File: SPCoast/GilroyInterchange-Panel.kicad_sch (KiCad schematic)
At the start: 17 parts, among them U6023 0x22, U6024 0x23

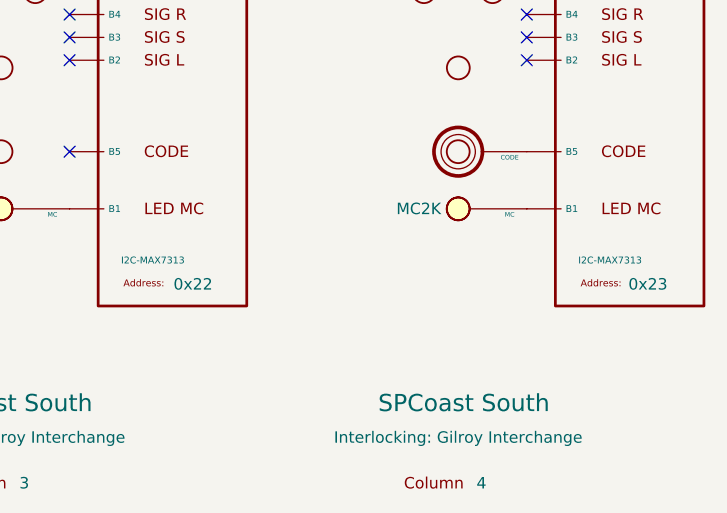
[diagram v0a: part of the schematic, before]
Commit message: chore(kicad): SPCoast symbols refreshed, field attribute visibility, no-connects on unused pins (owner's edit, baseline)
Owner, 2026-10-08: updated symbols from the libraries (the field pin direction flip, InterlockingPlant
61269e0), adjusted attribute visibility, added 22 no-connect markers on unused pins.

Verified (committed as saved, no edits):
- 485 components, 648 nets; every net identical to the previous commit.
- ERC 53 -> 20 messages (13 errors, 7 warnings). Remaining: unconnected HOUSE H / aux MC pins
  (Gilroy Caltrain, Luchessa, Watsonville); Corporal SW11901 still Railroad:Switch_HandThrow (not in
  the library) with open N/R legs; Sargent switch 1 open N/R legs; Christopher Panel U10029 A6 open
  while lamp LMP10093 carries a no-connect; 5 inherited wire stubs.
- Every instance path starts at the root uuid.

Co-Authored-By: Claude Opus 5.5 <noreply@anthropic.com>
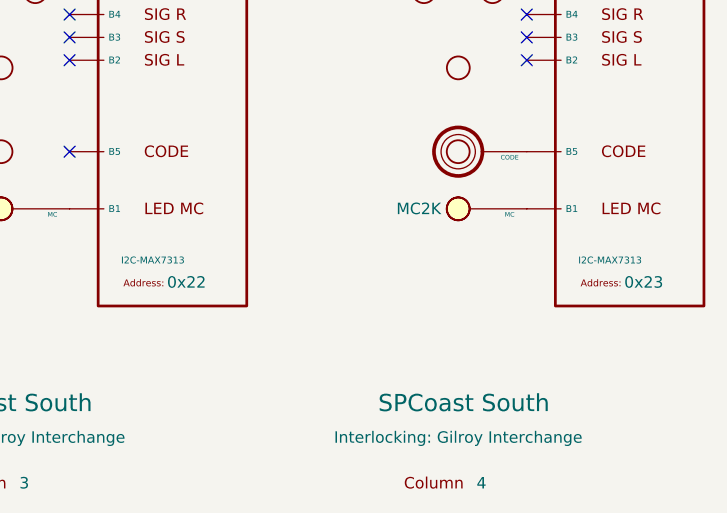
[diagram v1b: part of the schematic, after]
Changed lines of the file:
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@@
+			)
+		)
+		(property "LAMP" ""
+			(at 130.81 26.67 0)
+			(hide yes)
+			(show_name no)
+			(do_not_autoplace no)
+			(effects
+				(font
+					(size 1.27 1.27)
+				)
 			)
 		)
@@
 			)
 		)
+		(property "LAMP" ""
+			(at 80.01 31.75 0)
+			(hide yes)
+			(show_name no)
+			(do_not_autoplace no)
+			(effects
+				(font
+					(size 1.27 1.27)
+				)
+			)
+		)
 		(pin "1"
 		)
@@
 			)
 		)
+		(property "CODE" ""
+			(at 130.81 97.79 0)
+			(hide yes)
+			(show_name no)
+			(do_not_autoplace no)
+			(effects
+				(font
+					(size 1.27 1.27)
+				)
+			)
+		)
 		(pin "1"
 		)
@@
 			)
 		)
+		(property "LAMP" ""
+			(at 80.01 36.83 0)
+			(hide yes)
+			(show_name no)
+			(do_not_autoplace no)
+			(effects
+				(font
+					(size 1.27 1.27)
+				)
+			)
+		)
 		(pin "1"
 		)
@@
 			)
 		)
+		(property "LAMP" ""
+			(at 130.81 104.14 0)
+			(hide yes)
+			(show_name no)
+			(do_not_autoplace no)
+			(effects
+				(font
+					(size 1.27 1.27)
+				)
+			)
+		)
 		(pin "1"
 		)
@@
 			)
 		)
+		(property "WLS" ""
+			(at 130.81 63.5 0)
+			(hide yes)
+			(show_name no)
+			(do_not_autoplace no)
+			(effects
+				(font
+					(size 1.27 1.27)
+				)
+			)
+		)
+		(property "WLK" ""
+			(at 130.81 63.5 0)
+			(hide yes)
+			(show_name no)
+			(do_not_autoplace no)
+			(effects
+				(font
+					(size 1.27 1.27)
+				)
+			)
+		)
 		(pin "1"
 		)
@@
 			)
 		)
+		(property "WLS" ""
+			(at 80.01 63.5 0)
+			(hide yes)
+			(show_name no)
+			(do_not_autoplace no)
+			(effects
+				(font
+					(size 1.27 1.27)
+				)
+			)
+		)
+		(property "WLK" ""
+			(at 80.01 63.5 0)
+			(hide yes)
+			(show_name no)
+			(do_not_autoplace no)
+			(effects
+				(font
+					(size 1.27 1.27)
+				)
+			)
+		)
 		(pin "1"
 		)
@@
 			)
 		)
+		(property "LAMP" ""
+			(at 130.81 36.83 0)
+			(hide yes)
+			(show_name no)
+			(do_not_autoplace no)
+			(effects
+				(font
+					(size 1.27 1.27)
+				)
+			)
+		)
 		(pin "1"
 		)
@@
 			)
 		)
+		(property "SW" ""
+			(at 80.01 48.26 0)
+			(hide yes)
+			(show_name no)
+			(do_not_autoplace no)
+			(effects
+				(font
+					(size 1.27 1.27)
+				)
+			)
+		)
 		(pin "1"
 		)
@@
 			)
 		)
+		(property "LAMP" ""
+			(at 80.01 26.67 0)
+			(hide yes)
+			(show_name no)
+			(do_not_autoplace no)
+			(effects
+				(font
+					(size 1.27 1.27)
+				)
+			)
+		)
 		(pin "1"
 		)
@@
 			(at 144.145 109.855 0)
 			(show_name no)
-			(do_not_autoplace no)
+			(do_not_autoplace yes)
 			(effects
 				(font
@@
 		)
 		(property "Address" "0x23"
-			(at 151.892 112.522 0)
+			(at 151.4281 112.3109 0)
 			(show_name no)
 			(do_not_autoplace no)
@@
 			(at 93.345 109.855 0)
 			(show_name no)
-			(do_not_autoplace no)
+			(do_not_autoplace yes)
 			(effects
 				(font
@@
 		)
 		(property "Address" "0x22"
-			(at 101.346 112.522 0)
+			(at 100.6281 112.3109 0)
 			(show_name no)
 			(do_not_autoplace no)
@@
 			)
 		)
+		(property "LAMP" ""
+			(at 80.01 104.14 0)
+			(hide yes)
+			(show_name no)
+			(do_not_autoplace no)
+			(effects
+				(font
+					(size 1.27 1.27)
+				)
+			)
+		)
 		(pin "1"
 		)
@@
 			)
 		)
+		(property "LAMP" ""
+			(at 130.81 31.75 0)
+			(hide yes)
+			(show_name no)
+			(do_not_autoplace no)
+			(effects
+				(font
+					(size 1.27 1.27)
+				)
+			)
+		)
 		(pin "1"
 		)
@@
 			)
 		)
+		(property "SW" ""
+			(at 130.81 48.26 0)
+			(hide yes)
+			(show_name no)
+			(do_not_autoplace no)
+			(effects
+				(font
+					(size 1.27 1.27)
+				)
+			)
+		)

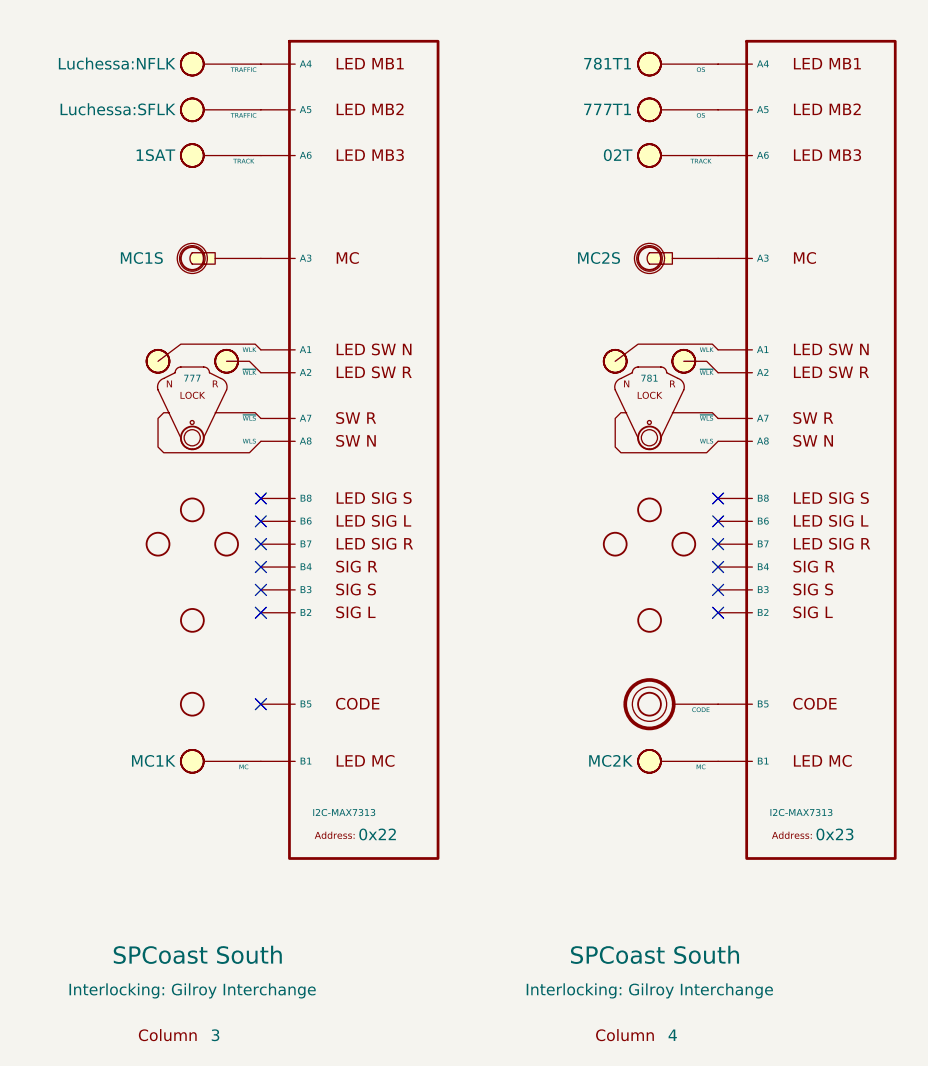
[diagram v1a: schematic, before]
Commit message: feat(spcoast): every sheet on the four Railroad libraries (checkpoint step 6, mechanical half)
By SPCoast/edits/2026-10-12-migrate-libraries.py, run once with KiCad closed: 483 instances
remapped across 16 sheets, embedded definitions replaced by the library blocks, instance fields
synced (Kind, ControlToken, Vital, NormalIs, Chain, Index dropped; Indications renamed
IndicationCeiling; Hold_ms renamed hold_ms; a pixel's Index became its Address; Rulebook kept
on the four Luchessa markers because the compiler still reads it), and 22 units added at the
same position for the plates and devices that are multi-unit now. Owner's choices: every plant
head CPL; Sargent's semaphore UQ; the 0x27 PCA9685 as PWM; the office MAX7313s as the
SPCoastcTc variant. Left by hand: the two AUXILIARY_TRAFFIC markers on Watsonville (retired).

Verified (production/migration-gate.txt, netlist_diff.py against pre-migration.net): office
and local plates and all chips keep their connectivity; 14 nets lost, all on Sargent, where
the six field devices (DevSW13001, 13004 to 13007, 13012) have new pin positions and must be
re-wired by hand. ERC: lib_symbol_issues 492 before (unregistered libraries) to 2 after (the
retired markers); the 29 unconnected pins are those devices and their chip pins.

Co-Authored-By: Claude Fable 5.1 <noreply@anthropic.com>
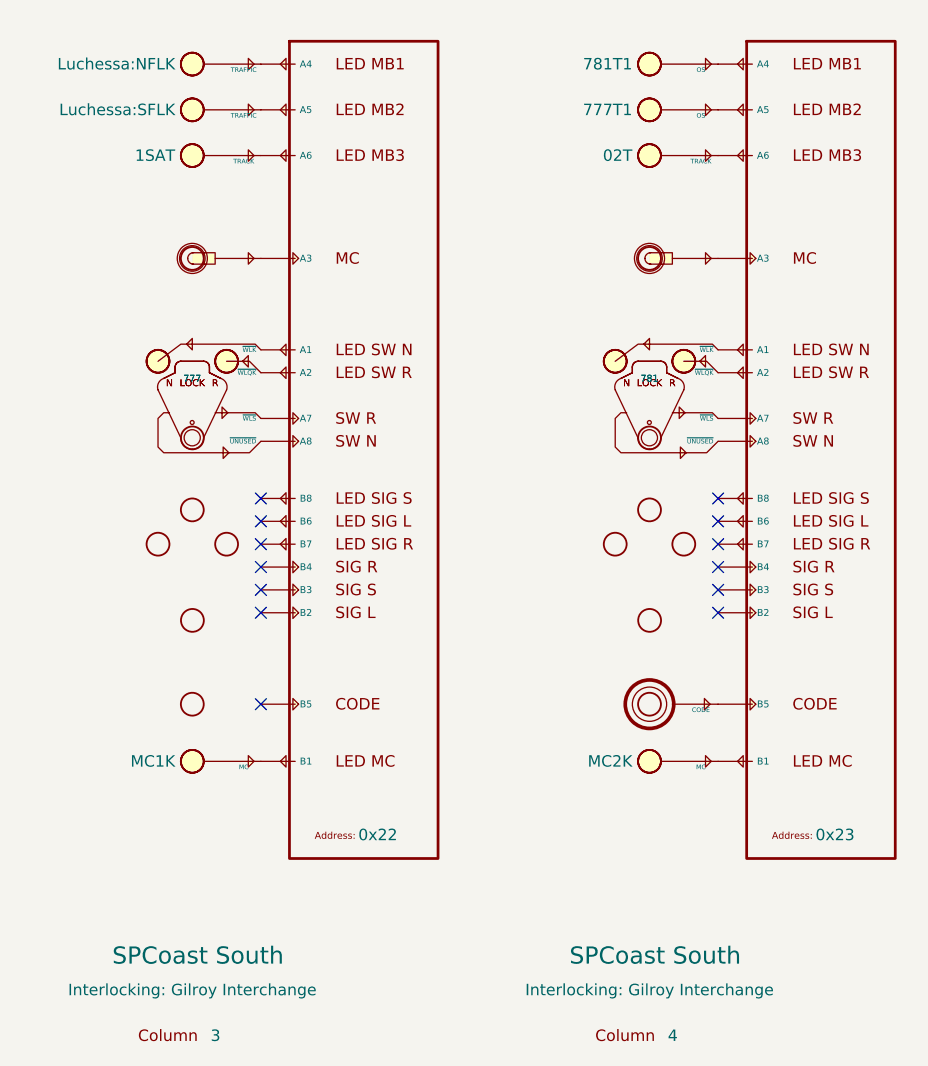
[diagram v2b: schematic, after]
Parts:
- added unit 2 of LKL6003
- added unit 2 of LKL6004
- CDE6004: symbol RailroadPanel:PanelCode -> Railroad-Office:PanelCode; Appliance (none) -> lever; Kind CODE -> (none); Pin.CODE (none) -> binary; Style (none) -> code
- COL6023, COL6024: symbol RailroadPanel:PanelColumn -> Railroad-Office:PanelColumn
- LKL6003, LKL6004: symbol RailroadPanel:PanelLock -> Railroad-Office:PanelLock; Appliance (none) -> lever; Invert (none) -> WLK; Kind LOCK_LEVER_2LAMP_2CONTACT -> (none); Pin.UNUSED (none) -> binary; Pin.WLK (none) -> binary; Pin.WLQK (none) -> binary; Pin.WLS (none) -> binary; Style (none) -> lock
- LMP6031, LMP6032: symbol RailroadPanel:PanelLamp-BLUE -> Railroad-Office:PanelLamp-BLUE; Appliance (none) -> lamp; Kind LAMP -> (none); Pin.LAMP (none) -> binary; Style (none) -> indication
- LMP6033, LMP6041, LMP6042, LMP6043, MCK6003, MCK6004: symbol RailroadPanel:PanelLamp-YELLOW -> Railroad-Office:PanelLamp-YELLOW; Appliance (none) -> lamp; Kind LAMP -> (none); Pin.LAMP (none) -> binary; Style (none) -> indication
- MCL6003: symbol RailroadPanel:PanelMCall -> Railroad-Office:PanelMCall; Appliance (none) -> lever; ControlToken MC1S -> (none); Kind MAINTAINER_CALL -> (none); Pin.S (none) -> binary; Style (none) -> maintainer_call; Vital NO -> (none)
- MCL6004: symbol RailroadPanel:PanelMCall -> Railroad-Office:PanelMCall; Appliance (none) -> lever; ControlToken MC2S -> (none); Kind MAINTAINER_CALL -> (none); Pin.S (none) -> binary; Style (none) -> maintainer_call; Vital NO -> (none)
- U6023, U6024: symbol RailroadPanel:Driver-I2C-MAX7313 -> Railroad-HardwareIO:Driver-I2C-MAX7313-SPCoastcTc; IC (none) -> MAX7313; Kind I2C-MAX7313 -> (none); Pin.A1 (none) -> binary; Pin.A2 (none) -> binary; Pin.A3 (none) -> binary; Pin.A4 (none) -> binary; Pin.A5 (none) -> binary; Pin.A6 (none) -> binary; Pin.A7 (none) -> binary; Pin.A8 (none) -> binary; Pin.B1 (none) -> binary; Pin.B2 (none) -> binary; Pin.B3 (none) -> binary; Pin.B4 (none) -> binary; Pin.B5 (none) -> binary; Pin.B6 (none) -> binary; Pin.B7 (none) -> binary; Pin.B8 (none) -> binary
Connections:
- net at U6024.2 (A2): now also LKL6004.4 (~{WLQK}); no longer LKL6004.4 (~{WLK})
- net at U6024.1 (A1): now also LKL6004.5 (~{WLK}); no longer LKL6004.5 (WLK)
- net at U6023.2 (A2): now also LKL6003.4 (~{WLQK}); no longer LKL6003.4 (~{WLK})
- net at U6023.1 (A1): now also LKL6003.5 (~{WLK}); no longer LKL6003.5 (WLK)

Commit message: chore: owner's Sargent cleanup and library edits of 2026-10-12 and 13 (baseline)
Co-Authored-By: Claude Fable 5.1 <noreply@anthropic.com>
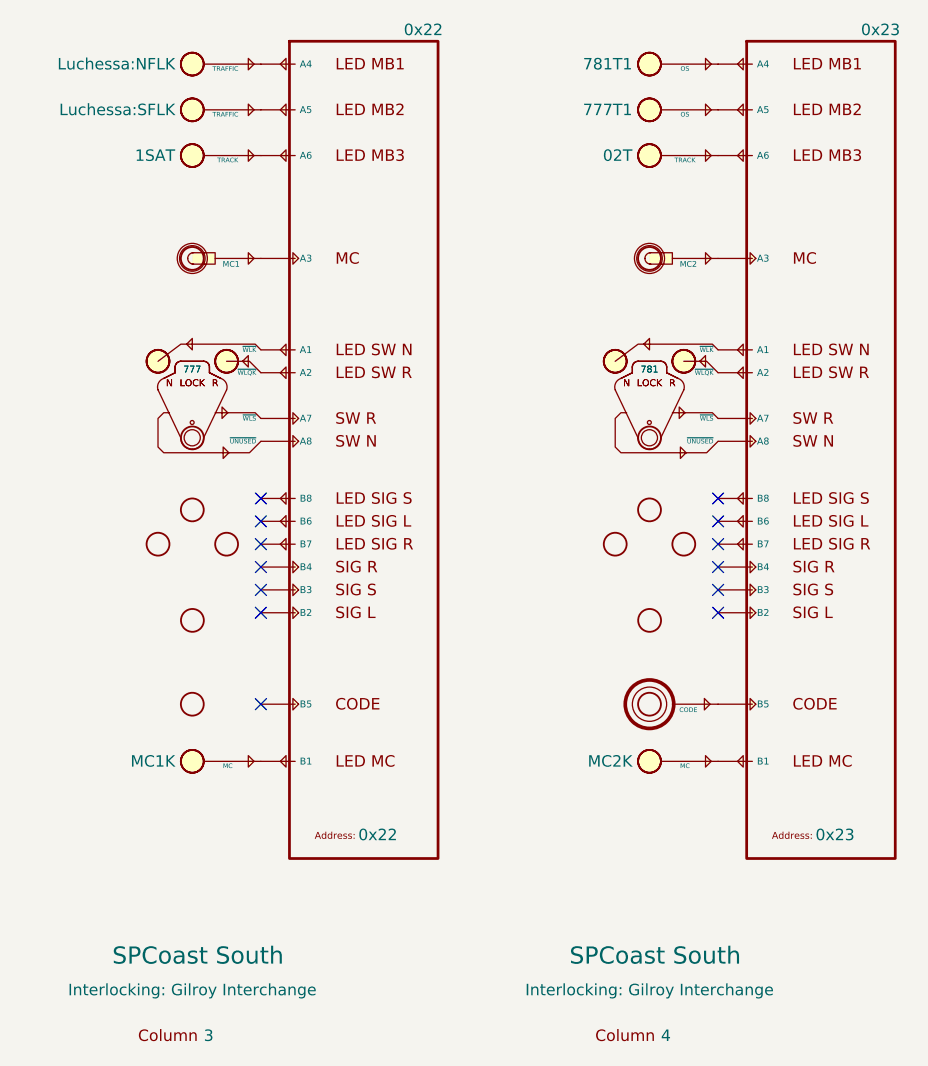
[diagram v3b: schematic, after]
